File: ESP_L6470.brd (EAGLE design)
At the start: 41.9 x 91.4 mm, 33 parts, among them J2 POWER_JACKPTH_LOCK, Q1 600mA/40V, Q2 600mA/40V, U1 L6470, U2 ESP-WROOM-03, U3 WS2811

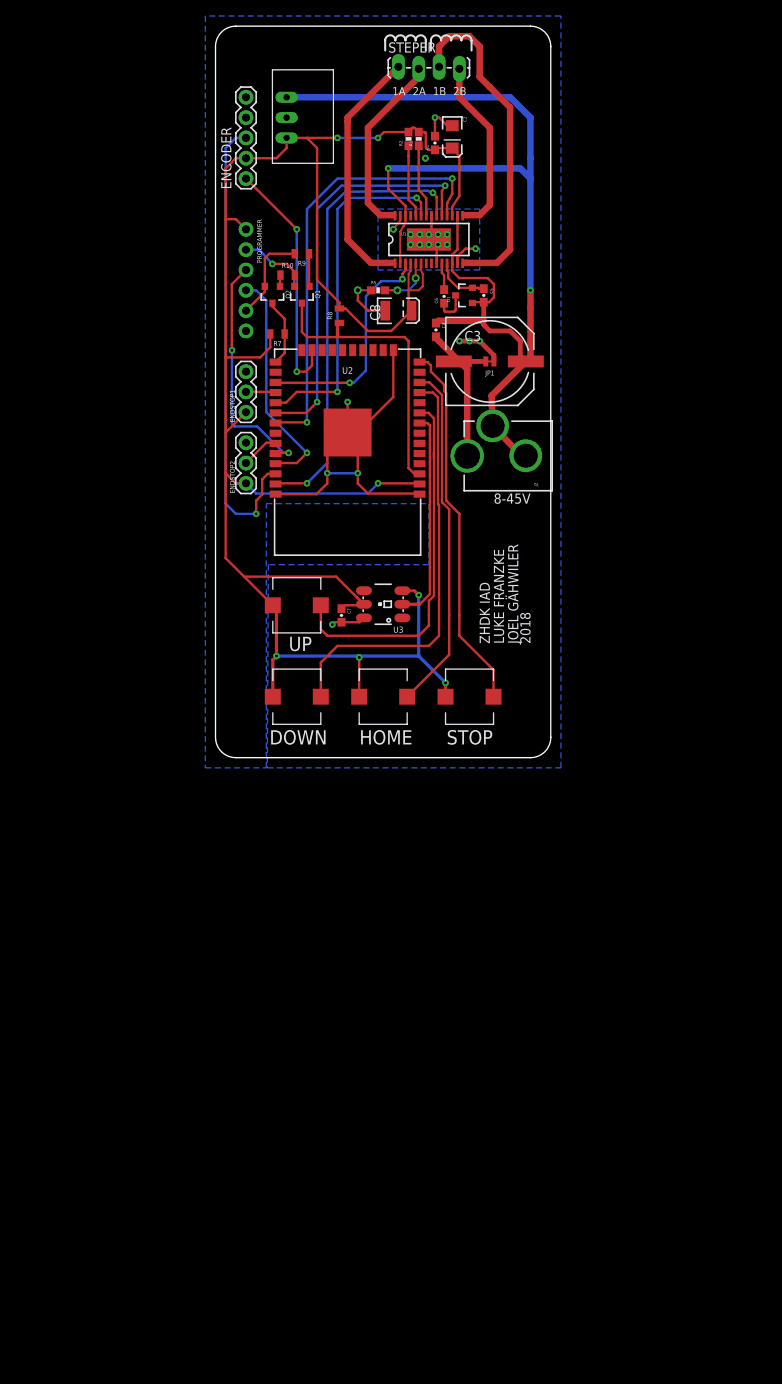
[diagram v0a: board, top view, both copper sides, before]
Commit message: Update schematic with USB to Serial
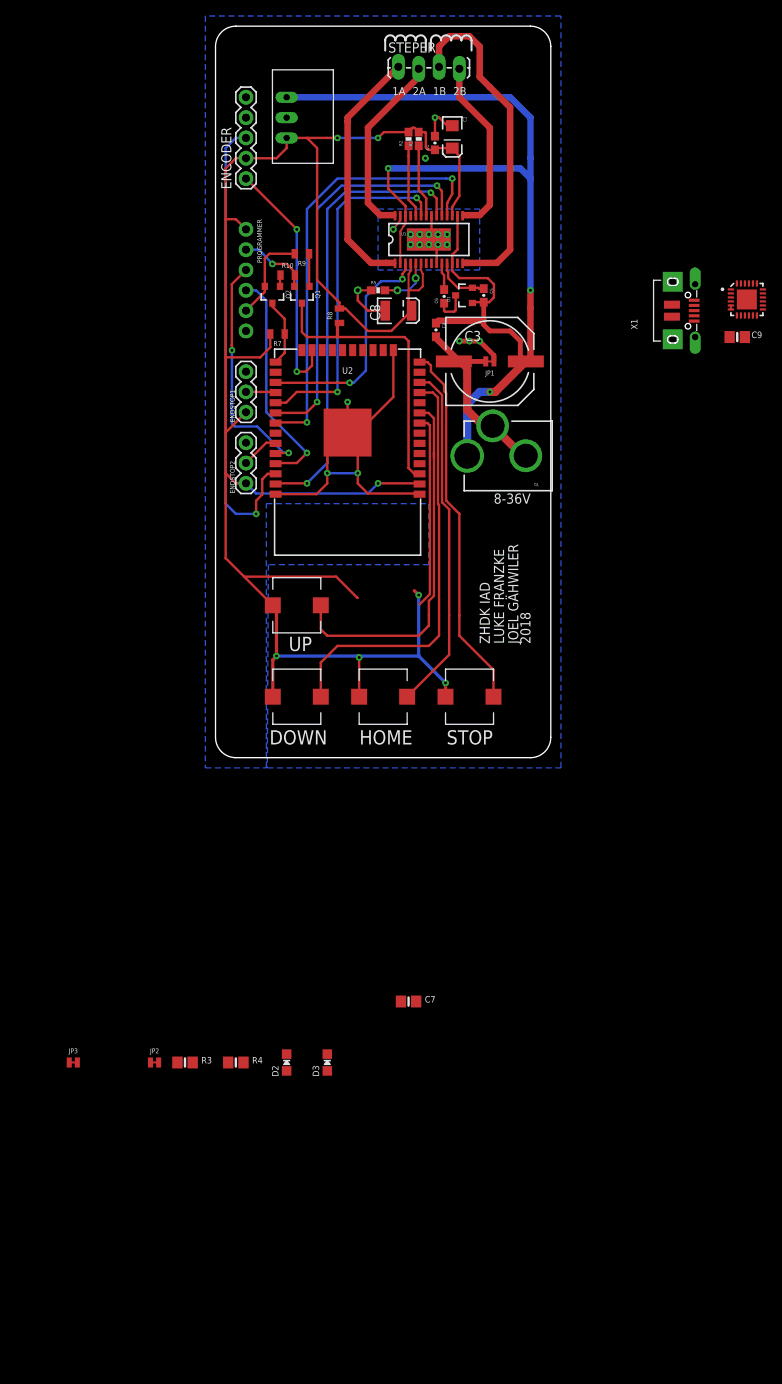
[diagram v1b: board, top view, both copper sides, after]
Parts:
- removed U3: WS2811, SparkFun-LED:LED-TRICOLOR-5050-IC
- added C9: 10uF, microbuilder:0805-NO
- added D2: RED, microbuilder:CHIPLED_0805_NOOUTLINE
- added D3: GREEN, microbuilder:CHIPLED_0805_NOOUTLINE
- added IC2: CP2104, microbuilder:QFN24_4MM_SMSC
- added JP2, JP3: JUMPER-SMT_2_NC_TRACE_NO-SILK, SparkFun-Jumpers:SMT-JUMPER_2_NC_TRACE_NO-SILK
- added R3, R4: 1K, microbuilder:0805-NO
- added X1: 20329, microbuilder:4UCONN_20329_V2
- C7: value 0.1uF -> 10uF; device SparkFun-Capacitors:0603-CAP -> microbuilder:0805-NO
- moved C7 49.0 mm to (26.7, -29.2), turned to 0 degrees
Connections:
- net MC_EN renamed RESET
- new net N$1: U2.10
- new net N$10: U2.22
- new net N$13: IC2.3, X1.D+
- new net N$14: IC2.4, X1.D-
- new net N$15: C7.1, IC2.16
- new net N$16: D2.A, R3.1
- new net N$17: D3.A, R4.1
- new net N$18: D2.C, IC2.14
- new net N$19: D3.C, IC2.13
- new net N$2: U2.17
- new net N$3: U2.18
- new net N$4: U2.19
- new net N$5: U2.20
- new net N$6: U2.21
- new net RXD0: IC2.21, JP2.1
- new net TP: IC2.THERM
- new net TXD0: IC2.20, JP3.1
- new net VBUS: IC2.8, X1.VBUS
- net 3.3V: now also C9.1, IC2.5, IC2.6, IC2.7, R3.2, R4.2; no longer C7.1, U3.3, U3.5
- net DTR: now also IC2.23
- net GND: now also C9.2, IC2.2, X1.BASE@1, X1.BASE@2, X1.GND, X1.SPRT@1, X1.SPRT@2, X1.SPRT@3, X1.SPRT@4; no longer U3.6
- net NEOPIXEL: no longer U3.2
- net PGND: now also J2.GND, J2.GNDBREAK; no longer J2.PWR
- net RTS: now also IC2.19
- net RX: now also JP3.2
- net TX: now also JP2.2
- net VS: now also J2.PWR; no longer J2.GND, J2.GNDBREAK
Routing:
- net GND: track 79.0 -> 71.2 mm, vias 22 -> 20
- net 3.3V: track 255.1 -> 249.9 mm
- net PGND: track 20.5 -> 24.4 mm
- net NEOPIXEL: track 26.5 -> 24.3 mm
- net SCK: track 50.9 -> 50.0 mm
- net SDI: track 57.0 -> 56.3 mm
- net VS: track 144.5 -> 144.9 mm, vias 2 -> 3
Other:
- board text added: "8-36V"
- board text removed: "8-45V"

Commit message: added some components
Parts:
- added J1: MICRO-USB, SparkFun-Connectors:USB-MICROB
- added R11, R12, R6: 1k, SparkFun-Resistors:0603
- added U3: RGB-LED, Particle:PLCC4-2MM-RGB
- added U7: CP2104, microbuilder:QFN24_4MM_SMSC
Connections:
- new net BLUE: R12.2
- new net GREEN: R11.2
- new net N$11: R11.1, U3.GREEN
- new net N$12: R6.1, U3.RED
- new net N$20: R12.1, U3.BLUE
- new net RED: R6.2
- new net REGIN: U7.7
- new net VDD: U7.6
- new net VIO: U7.5
- net 3.3V: now also U3.CA
- net GND: now also J1.GND, U7.2
- net TP: now also U7.THERM
- net VBUS: now also J1.VBUS, U7.8
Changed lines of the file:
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@@
 <layer number="59" name="tCarbon" color="7" fill="1" visible="no" active="no"/>
 <layer number="60" name="bCarbon" color="7" fill="1" visible="no" active="no"/>
+<layer number="88" name="SimResults" color="9" fill="1" visible="no" active="no"/>
+<layer number="89" name="SimProbes" color="9" fill="1" visible="no" active="no"/>
 <layer number="90" name="Modules" color="5" fill="1" visible="no" active="no"/>
 <layer number="91" name="Nets" color="2" fill="1" visible="no" active="no"/>
@@
 <element name="JP2" library="SparkFun-Jumpers" package="SMT-JUMPER_2_NC_TRACE_NO-SILK" value="JUMPER-SMT_2_NC_TRACE_NO-SILK" x="-5.08" y="-36.83"/>
 <element name="JP3" library="SparkFun-Jumpers" package="SMT-JUMPER_2_NC_TRACE_NO-SILK" value="JUMPER-SMT_2_NC_TRACE_NO-SILK" x="-15.24" y="-36.83"/>
+<element name="U7" library="microbuilder" package="QFN24_4MM_SMSC" value="CP2104" x="-19.05" y="-55.88"/>
+<element name="J1" library="SparkFun-Connectors" package="USB-MICROB" value="MICRO-USB" x="-19.05" y="-45.72">
+<attribute name="PROD_ID" value="CONN-09505" x="-26.67" y="-41.91" size="1.778" layer="27" display="off"/>
+<attribute name="SF_ID" value="PRT-08533" x="-26.67" y="-41.91" size="1.778" layer="27" display="off"/>
+</element>
+<element name="U3" library="Particle" package="PLCC4-2MM-RGB" value="RGB-LED" x="-20.32" y="-73.66"/>
+<element name="R6" library="SparkFun-Resistors" package="0603" value="1k" x="-20.32" y="-62.23">
+<attribute name="PROD_ID" value="RES-07856" x="-20.32" y="-64.77" size="1.778" layer="27" display="off"/>
+</element>
+<element name="R11" library="SparkFun-Resistors" package="0603" value="1k" x="-20.32" y="-66.04">
+<attribute name="PROD_ID" value="RES-07856" x="-20.32" y="-68.58" size="1.778" layer="27" display="off"/>
+</element>
+<element name="R12" library="SparkFun-Resistors" package="0603" value="1k" x="-20.32" y="-69.85">
+<attribute name="PROD_ID" value="RES-07856" x="-20.32" y="-72.39" size="1.778" layer="27" display="off"/>
+</element>
 </elements>
 <signals>
@@
 <contactref element="C9" pad="2"/>
 <contactref element="C7" pad="2"/>
+<contactref element="U7" pad="2"/>
+<contactref element="J1" pad="GND"/>
 <wire x1="62.495" y1="60.45" x2="66.961" y2="59.297" width="0" layer="19" extent="1-1"/>
 <wire x1="59.695" y1="60.75" x2="62.495" y2="60.45" width="0" layer="19" extent="1-1"/>
@@
 <wire x1="6.35" y1="83.82" x2="11.43" y2="81.28" width="0" layer="19" extent="1-1"/>
 <wire x1="27.62" y1="-29.21" x2="28.05" y2="34.21" width="0" layer="19" extent="1-1"/>
+<wire x1="-21.7" y1="-44.42" x2="27.62" y2="-29.21" width="0" layer="19" extent="1-1"/>
+<wire x1="-21.05" y1="-55.13" x2="-21.7" y2="-44.42" width="0" layer="19" extent="1-1"/>
 </signal>
 <signal name="FLAGN">
@@
 <contactref element="R3" pad="2"/>
 <contactref element="R4" pad="2"/>
+<contactref element="U3" pad="CA"/>
 <wire x1="66.961" y1="57.297" x2="67.711" y2="56.547" width="0" layer="19" extent="1-1"/>
 <wire x1="66.8045" y1="53.848" x2="67.711" y2="56.547" width="0" layer="19" extent="1-1"/>
@@
 <wire x1="6.03" y1="-36.83" x2="9.7" y2="8.89" width="0" layer="19" extent="1-1"/>
 <wire x1="-0.32" y1="-36.83" x2="6.03" y2="-36.83" width="0" layer="19" extent="1-1"/>
+<wire x1="-19.57" y1="-74.21" x2="-0.32" y2="-36.83" width="0" layer="19" extent="1-1"/>
 </signal>
 <signal name="OSCIN">
@@
 <contactref element="IC2" pad="8"/>
 <contactref element="X1" pad="VBUS"/>
+<contactref element="U7" pad="8"/>
+<contactref element="J1" pad="VBUS"/>
 <wire x1="62.37" y1="58.45" x2="68.211" y2="56.547" width="0" layer="19" extent="1-1"/>
+<wire x1="-21.7" y1="-47.02" x2="62.37" y2="58.45" width="0" layer="19" extent="1-1"/>
+<wire x1="-19.8" y1="-57.88" x2="-21.7" y2="-47.02" width="0" layer="19" extent="1-1"/>
 </signal>
 <signal name="RXD0">
@@
 <signal name="TP">
 <contactref element="IC2" pad="THERM"/>
+<contactref element="U7" pad="THERM"/>
+<wire x1="-19.05" y1="-55.88" x2="68.961" y2="58.547" width="0" layer="19" extent="1-1"/>
 </signal>
 <signal name="N$15">
@@
 <wire x1="16.51" y1="-35.78" x2="70.961" y2="57.297" width="0" layer="19" extent="1-1"/>
 </signal>
+<signal name="VIO">
+<contactref element="U7" pad="5"/>
+</signal>
+<signal name="VDD">
+<contactref element="U7" pad="6"/>
+</signal>
+<signal name="REGIN">
+<contactref element="U7" pad="7"/>
+</signal>
+<signal name="RED">
+<contactref element="R6" pad="2"/>
+</signal>
+<signal name="GREEN">
+<contactref element="R11" pad="2"/>
+</signal>
+<signal name="BLUE">
+<contactref element="R12" pad="2"/>
+</signal>
+<signal name="N$11">
+<contactref element="U3" pad="GREEN"/>
+<contactref element="R11" pad="1"/>
+<wire x1="-21.17" y1="-66.04" x2="-21.07" y2="-73.11" width="0" layer="19" extent="1-1"/>
+</signal>
+<signal name="N$12">
+<contactref element="U3" pad="RED"/>
+<contactref element="R6" pad="1"/>
+<wire x1="-21.17" y1="-62.23" x2="-19.57" y2="-73.11" width="0" layer="19" extent="1-1"/>
+</signal>
+<signal name="N$20">
+<contactref element="R12" pad="1"/>
+<contactref element="U3" pad="BLUE"/>
+<wire x1="-21.17" y1="-69.85" x2="-21.07" y2="-74.21" width="0" layer="19" extent="1-1"/>
+</signal>
 </signals>

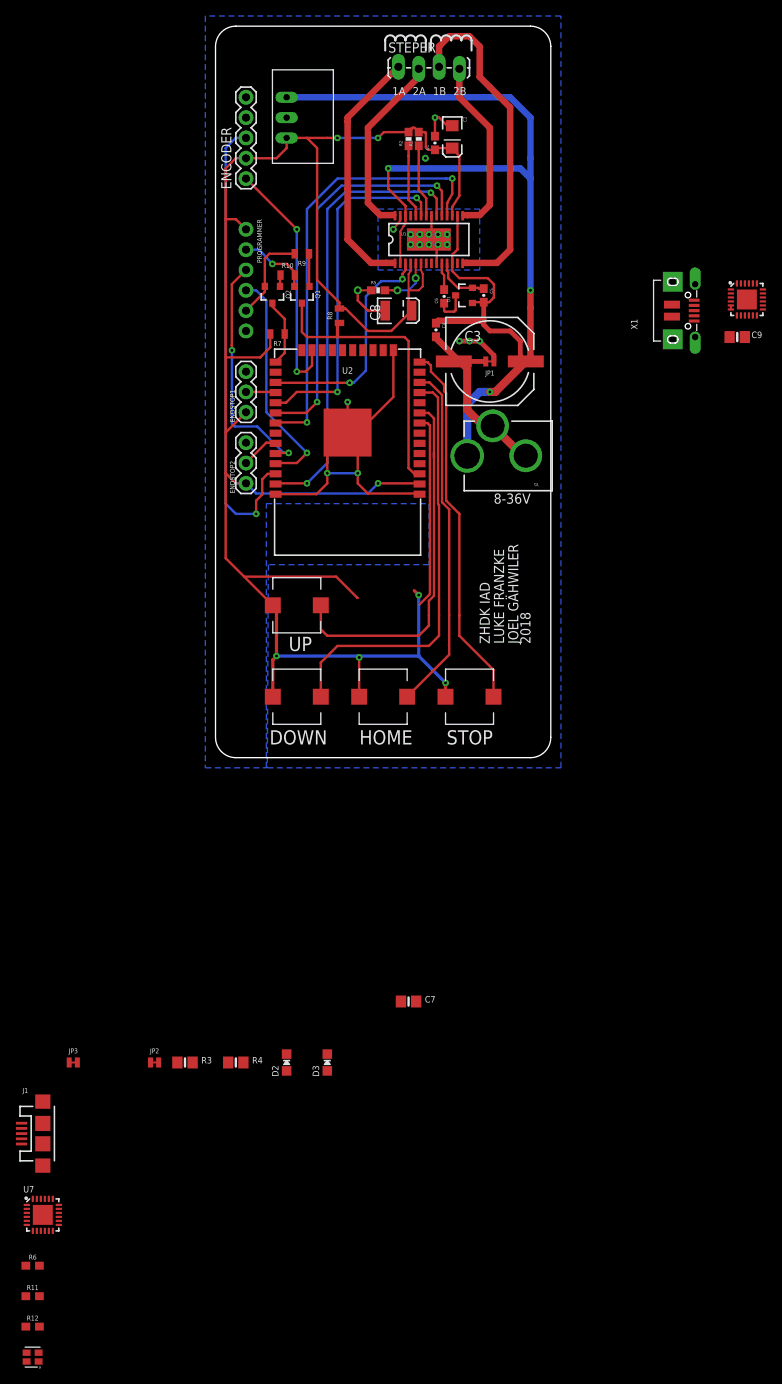
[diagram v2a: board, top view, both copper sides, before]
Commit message: update with USB to Serial
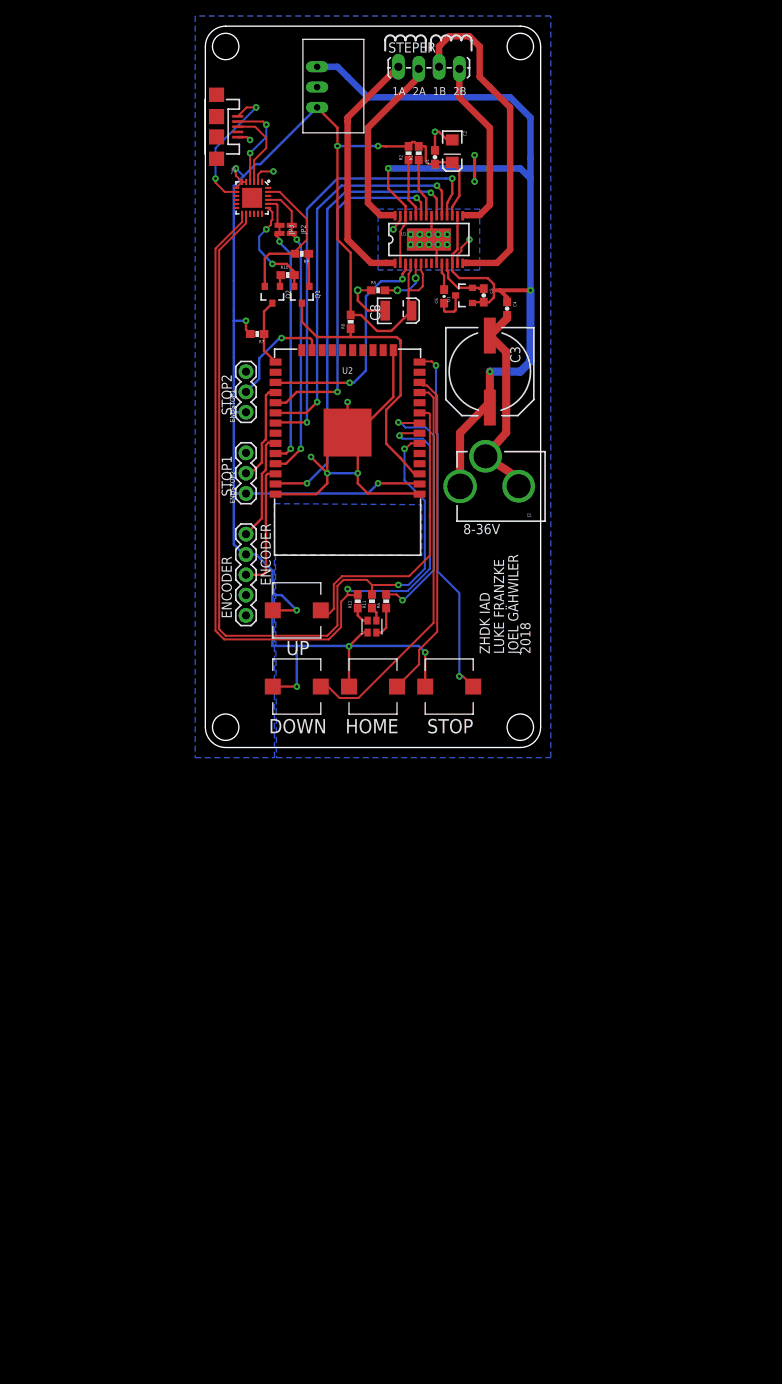
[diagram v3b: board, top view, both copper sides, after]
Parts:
- removed C7, C9: 10uF, microbuilder:0805-NO
- removed D2: RED, microbuilder:CHIPLED_0805_NOOUTLINE
- removed D3: GREEN, microbuilder:CHIPLED_0805_NOOUTLINE
- removed JP1: JUMPER-SMT_2_NC_TRACE_NO-SILK, SparkFun-Jumpers:SMT-JUMPER_2_NC_TRACE_NO-SILK
- removed PROGRAMMER: (no value), SparkFun-Connectors:1X06_NO_SILK
- removed R3, R4: 1K, microbuilder:0805-NO
- removed U7: CP2104, microbuilder:QFN24_4MM_SMSC
- removed X1: 20329, microbuilder:4UCONN_20329_V2
- added U$10, U$11, U$12, U$9: (no value), RP400N501A:STAND-OFF
- C1, C4, C5: device SparkFun-Capacitors:0603-CAP -> SparkFun-Passives:0603-CAP
- R1, R2, R5: device SparkFun-Resistors:0603-RES -> SparkFun-Passives:0603-RES
- R10, R7, R8, R9: device SparkFun-Resistors:0805 -> SparkFun-Passives:0603-RES
- R11, R12, R6: device SparkFun-Resistors:0603 -> SparkFun-Passives:0603-RES
- moved J1 127.7 mm to (2.67, 80.1), turned to 180 degrees
- moved JP3 107.3 mm to (10.5, 67.3), turned to 270 degrees
- moved JP2 105.5 mm to (12.1, 67.3), turned to 270 degrees
- moved U3 100.7 mm to (22.1, 17.7), turned to 270 degrees
- moved R12 99.4 mm to (20.3, 20.8), turned to 90 degrees
- moved R11 96.7 mm to (22.1, 20.8), turned to 90 degrees
- moved R6 94.1 mm to (23.9, 20.8), turned to 90 degrees
- moved IC2 63.1 mm to (7.11, 71.2), turned to 270 degrees
- moved ENCODER 44.4 mm to (6.35, 29.2), turned to 270 degrees
- moved C4 9.28 mm to (39.0, 57.4)
- moved U$5 5.39 mm to (15.2, 85.1)
- moved J2 3.91 mm to (47.0, 35.2)
- moved U$24 2.84 mm to (31.8, 10.2)
- moved R7 2.54 mm to (7.75, 54.2)
- moved U$23 1.80 mm to (22.2, 10.2)
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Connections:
- removed net N$15: C7.1, IC2.16
- removed net N$16: D2.A, R3.1
- removed net N$17: D3.A, R4.1
- removed net N$18: D2.C, IC2.14
- removed net N$19: D3.C, IC2.13
- removed net N$7: U2.7
- removed net N6: U2.6
- removed net NEOPIXEL: U2.8
- removed net PGND: C3.-, C4.2, J2.GND, J2.GNDBREAK, JP1.2
- removed net REGIN: U7.7
- removed net VDD: U7.6
- removed net VIO: U7.5
- new net N$100: U2.16
- new net N$101: U2.32
- net 3.3V: no longer C9.1, PROGRAMMER.1, R3.2, R4.2
- net BLUE: now also IC2.13, U2.7
- net DTR: no longer PROGRAMMER.5
- net ENC_A: now also U2.33; no longer U2.23
- net ENDSTOP1: now also U2.23; no longer U2.28
- net ENDSTOP2: now also U2.28; no longer U2.33
- net GND: now also C3.-, C4.2, J2.GND, J2.GNDBREAK; no longer C7.2, C9.2, JP1.1, PROGRAMMER.6, U7.2, X1.BASE@1, X1.BASE@2, X1.GND, X1.SPRT@1, X1.SPRT@2, X1.SPRT@3, X1.SPRT@4
- net GREEN: now also IC2.14, U2.6
- net N$13: now also J1.D+; no longer X1.D+
- net N$14: now also J1.D-; no longer X1.D-
- net RED: now also U2.8
- net RTS: no longer PROGRAMMER.2
- net RX: no longer PROGRAMMER.3
- net TP: no longer U7.THERM
- net TX: no longer PROGRAMMER.4
- net VBUS: no longer U7.8, X1.VBUS
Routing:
- net BLUE: track 0.00 -> 110.9 mm, vias 0 -> 2
- net GREEN: track 0.00 -> 105.8 mm, vias 0 -> 2
- net ENC_B: track 58.4 -> 16.0 mm, vias 1 -> 0
- net GND: track 71.2 -> 106.0 mm, vias 20 -> 22
- net RED: track 0.00 -> 32.6 mm, vias 0 -> 2
- net PGND: track 24.4 -> 0.00 mm
- net NEOPIXEL: track 24.3 -> 0.00 mm
- net 3.3V: track 249.9 -> 227.9 mm, vias 7 -> 9
- net ENC_A: track 30.9 -> 13.5 mm, vias 2 -> 0
- net VBUS: track 0.00 -> 17.3 mm, vias 0 -> 2
- net N$14: track 0.00 -> 11.7 mm, vias 0 -> 2
- net N$13: track 0.00 -> 10.3 mm
- net ENDSTOP1: track 3.73 -> 13.9 mm, vias 0 -> 1
- net UP: track 46.3 -> 38.3 mm
- net ENDSTOP2: track 4.79 -> 12.6 mm
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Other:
- board size 41.9 x 91.4 mm -> 41.9 x 90.2 mm
- board text added: "ENCODER"
- board text added: "STOP1"
- board text added: "STOP2"
